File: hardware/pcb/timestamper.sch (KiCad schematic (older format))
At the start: 107 parts, among them J1 Conn_Coaxial, J2 Conn_Coaxial, J3 Conn_Coaxial, J4 JTAG, J5 ISP, J6 Conn_Coaxial, J7 Micro_usb_B, U1 AP1117-33, U10 ATMEGA328-AU, U11 74HC04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

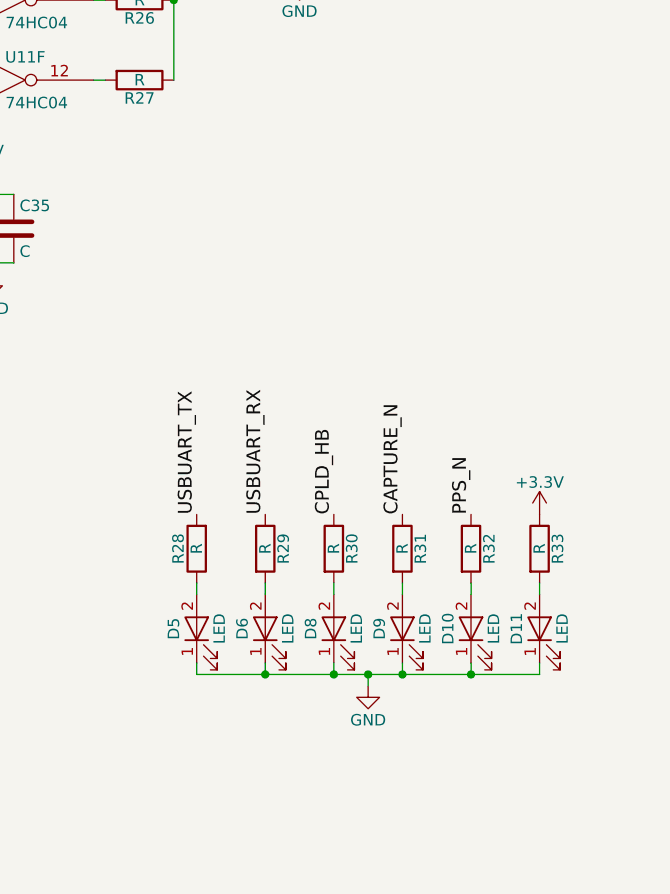
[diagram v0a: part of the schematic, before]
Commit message: Initial component placement
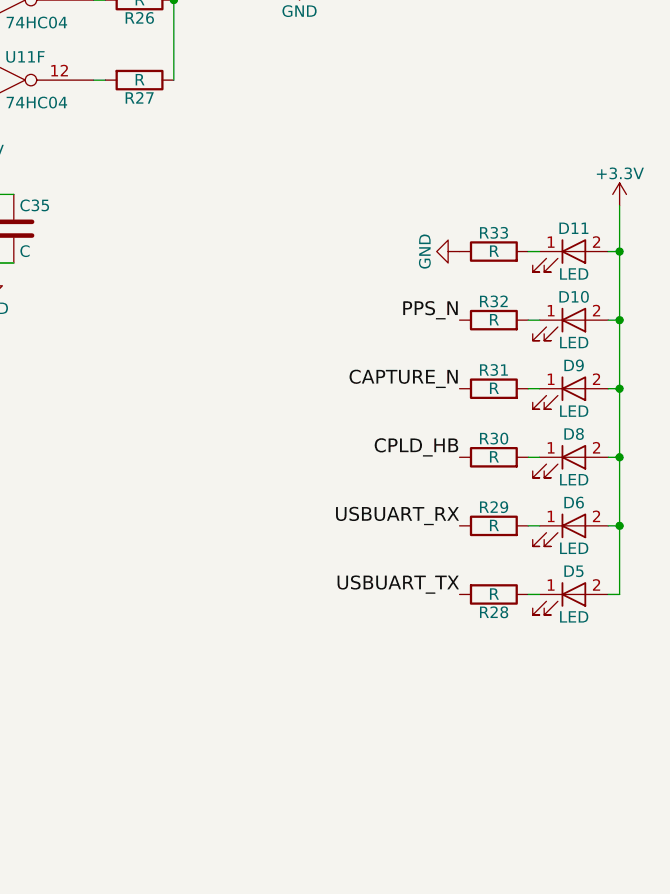
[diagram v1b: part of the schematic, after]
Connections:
- net +3V3: now also D10.2 (A), D11.2 (A), D5.2 (A), D6.2 (A), D8.2 (A), D9.2 (A); no longer R33.1
- net GND: now also R33.1; no longer D10.1 (K), D11.1 (K), D5.1 (K), D6.1 (K), D8.1 (K), D9.1 (K)
- net at R32.2: now also D10.1 (K); no longer D10.2 (A)
- net at R33.2: now also D11.1 (K); no longer D11.2 (A)
- net at R31.2: now also D9.1 (K); no longer D9.2 (A)
- net at R30.2: now also D8.1 (K); no longer D8.2 (A)
- net at R29.2: now also D6.1 (K); no longer D6.2 (A)
- net at R28.1: now also D5.1 (K); no longer D5.2 (A)
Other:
- moved on the sheet: D10, D11, D5, D6, D8, D9, R28, R29, R30, R31, R32, R33
